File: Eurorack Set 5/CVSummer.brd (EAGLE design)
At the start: 19 x 106.5 mm, 35 parts, among them IC2 TL074D

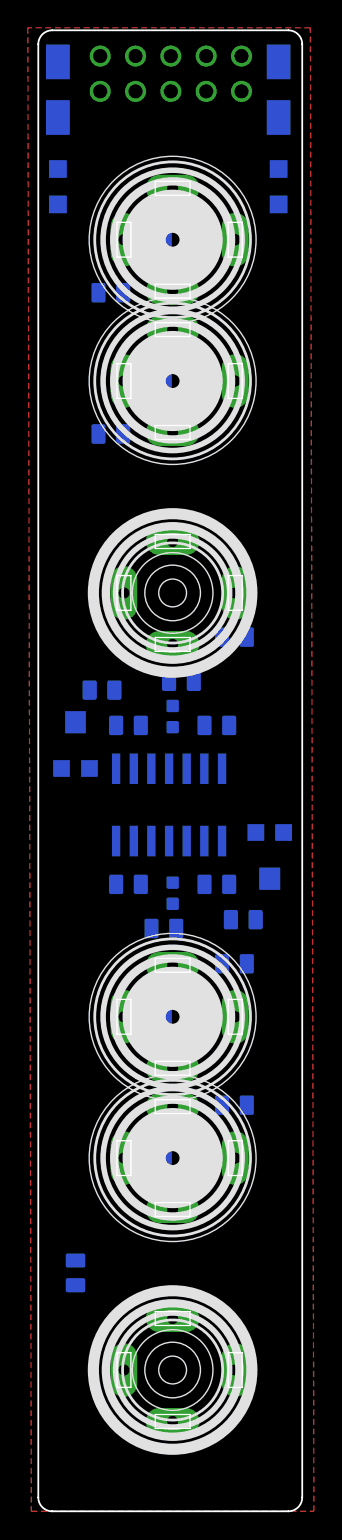
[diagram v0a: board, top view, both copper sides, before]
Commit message: Summer and Envelope updates (leftover opamp wiring)
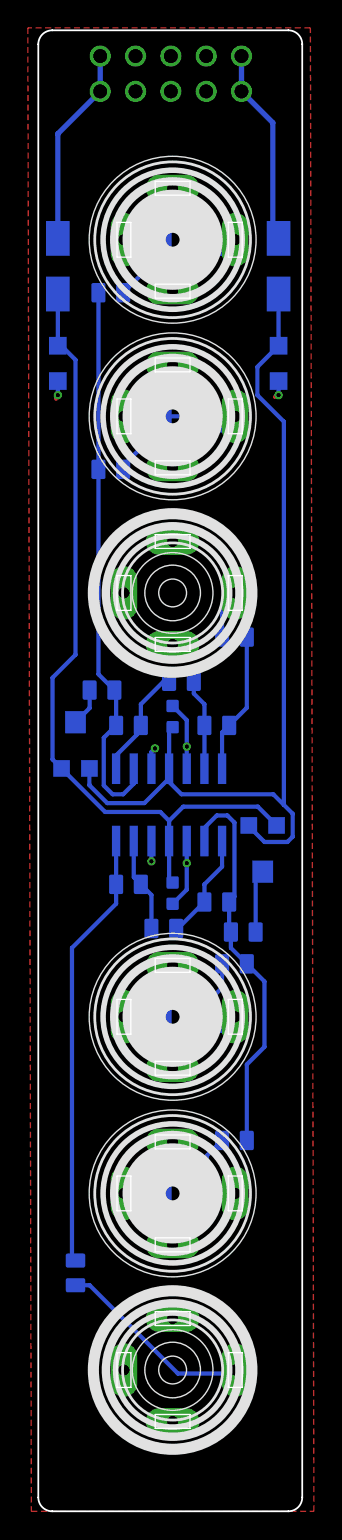
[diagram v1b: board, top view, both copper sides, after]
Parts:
- moved C11 12.7 mm to (1.91, 82.5)
- moved C12 12.7 mm to (17.8, 82.5)
- moved D1 12.7 mm to (1.91, 89.5)
- moved D2 12.7 mm to (17.8, 89.5)
- moved U$14 2.54 mm to (10.8, 78.7)
- moved U$2 2.54 mm to (10.2, 78.7)
- moved R8 2.54 mm to (14.6, 26.7)
- moved U$5 2.54 mm to (10.8, 22.9)
- moved U$6 2.54 mm to (10.2, 22.9)
- moved R5 2.54 mm to (5.71, 74.9)
- moved R2 1.27 mm to (13.3, 43.8)
- moved R6 0.89 mm to (15.2, 41.7)
- moved U$8 0.72 mm to (16.6, 47.5)
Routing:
- net -12V: track 0.00 -> 65.7 mm
- net 12V: track 0.00 -> 58.3 mm
- net N$14: track 0.00 -> 41.1 mm
- net N$5: track 0.00 -> 31.6 mm
- net N$13: track 0.00 -> 28.3 mm
- net GND: track 0.00 -> 15.7 mm, vias 0 -> 6
- net N$28: track 0.00 -> 14.4 mm
- net N$15: track 0.00 -> 14.2 mm
- net N$64: track 0.00 -> 14.2 mm
- net N$2: track 0.00 -> 10.2 mm
- net N$10: track 0.00 -> 8.66 mm
- net N$3: track 0.00 -> 8.66 mm
- net N$7: track 0.00 -> 8.09 mm
- net N$18: track 0.00 -> 7.73 mm
- net N$16: track 0.00 -> 7.00 mm
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
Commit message: Many tweaks for frontpanel setup
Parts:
- added SJ1, SJ2, SJ3, SJ4: SOLDERJUMPERNO, SparkFun-Passives:SJ_2S-NO
- moved C12 1.71 mm to (16.5, 83.7), turned to 180 degrees
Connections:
- new net N$20: SJ1.2, U$14.3, U$2.TIP@3
- new net N$21: SJ3.1, SJ4.1, U$3.SWITCH@3
- net GND: now also SJ2.1, SJ4.2; no longer U$3.SWITCH@3, U$6.SWITCH@3
- net N$1: now also SJ1.1, SJ2.2, U$6.SWITCH@3; no longer U$14.3, U$2.TIP@3
- net N$12: now also SJ3.2
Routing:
- net N$21: track 0.00 -> 68.1 mm, vias 0 -> 4
- net N$1: track 2.45 -> 67.6 mm, vias 0 -> 4
- net N$20: track 0.00 -> 5.40 mm
- net N$12: track 2.45 -> 5.23 mm
- net GND: track 15.7 -> 18.2 mm, vias 6 -> 8
- net -12V: track 65.7 -> 64.4 mm
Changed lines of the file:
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@@
 </element>
 <element name="C11" library="OPL" package="AVX-A" value="" x="1.905" y="82.55" rot="MR270"/>
-<element name="C12" library="OPL" package="AVX-A" value="" x="17.78" y="82.55" rot="MR90"/>
+<element name="C12" library="OPL" package="AVX-A" value="" x="16.51" y="83.693" rot="MR180"/>
 <element name="U$3" library="EurorackModularParts" package="3.5MM-JACK-SWITCH-13MM-INPUT" value="PJ-341" x="10.16" y="35.56" rot="R270">
 <attribute name="DESC" value="Input B" x="10.16" y="35.56" size="1.778" layer="27" rot="R270" display="off"/>
@@
 <element name="R13" library="OPL" package="C0805" value="100K" x="9.525" y="41.91" rot="MR0"/>
 <element name="R14" library="OPL" package="C0805" value="100K" x="6.985" y="45.085" rot="MR0"/>
+<element name="SJ1" library="SparkFun-Passives" package="SJ_2S-NO" value="SOLDERJUMPERNO" x="13.716" y="75.057" rot="MR0"/>
+<element name="SJ2" library="SparkFun-Passives" package="SJ_2S-NO" value="SOLDERJUMPERNO" x="6.731" y="19.05" rot="MR180"/>
+<element name="SJ3" library="SparkFun-Passives" package="SJ_2S-NO" value="SOLDERJUMPERNO" x="13.589" y="87.884" rot="MR0"/>
+<element name="SJ4" library="SparkFun-Passives" package="SJ_2S-NO" value="SOLDERJUMPERNO" x="6.731" y="31.877" rot="MR0"/>
 </elements>
 <signals>
@@
 <contactref element="IC2" pad="3"/>
 <contactref element="IC2" pad="5"/>
-<contactref element="U$6" pad="SWITCH@3"/>
 <contactref element="U$6" pad="RING@3"/>
 <contactref element="U$3" pad="RING@3"/>
-<contactref element="U$3" pad="SWITCH@3"/>
 <wire x1="11.176" y1="54.991" x2="11.176" y2="56.896" width="0.3048" layer="16"/>
 <wire x1="11.176" y1="56.896" x2="10.16" y2="57.912" width="0.3048" layer="16"/>
@@
 <wire x1="1.905" y1="80.264" x2="1.905" y2="80.137" width="0.3048" layer="1"/>
 <wire x1="1.905" y1="80.137" x2="1.778" y2="80.01" width="0.3048" layer="1"/>
-<wire x1="17.78" y1="81.28" x2="17.78" y2="80.264" width="0.3048" layer="16"/>
-<via x="17.78" y="80.264" extent="1-16" drill="0.3048"/>
-<wire x1="17.78" y1="80.264" x2="17.653" y2="80.264" width="0.3048" layer="1"/>
-<wire x1="17.653" y1="80.264" x2="17.526" y2="80.137" width="0.3048" layer="1"/>
+<wire x1="15.24" y1="83.693" x2="15.24" y2="84.836" width="0.3048" layer="16"/>
+<via x="15.24" y="84.836" extent="1-16" drill="0.3048"/>
+<wire x1="15.24" y1="84.836" x2="15.494" y2="85.09" width="0.3048" layer="1"/>
+<wire x1="15.494" y1="85.09" x2="15.24" y2="85.344" width="0.3048" layer="1"/>
+<contactref element="SJ2" pad="1"/>
+<contactref element="SJ4" pad="2"/>
+<wire x1="6.281" y1="31.877" x2="5.588" y2="31.877" width="0.3048" layer="16"/>
+<via x="5.588" y="31.877" extent="1-16" drill="0.3048"/>
+<wire x1="5.588" y1="31.877" x2="5.461" y2="31.877" width="0.3048" layer="1"/>
+<wire x1="5.461" y1="31.877" x2="5.334" y2="32.004" width="0.3048" layer="1"/>
+<wire x1="6.281" y1="19.05" x2="5.588" y2="19.05" width="0.3048" layer="16"/>
+<via x="5.588" y="19.05" extent="1-16" drill="0.3048"/>
+<wire x1="5.588" y1="19.05" x2="5.334" y2="19.05" width="0.3048" layer="1"/>
 </signal>
 <signal name="12V">
@@
 <wire x1="17.399" y1="51.562" x2="10.795" y2="51.562" width="0.3048" layer="16"/>
 <wire x1="10.795" y1="51.562" x2="9.779" y2="52.578" width="0.3048" layer="16"/>
-<wire x1="18.161" y1="50.8" x2="18.161" y2="78.359" width="0.3048" layer="16"/>
-<wire x1="17.78" y1="83.82" x2="17.78" y2="87.535" width="0.3048" layer="16"/>
-<wire x1="17.78" y1="83.82" x2="16.256" y2="82.296" width="0.3048" layer="16"/>
-<wire x1="16.256" y1="82.296" x2="16.256" y2="80.264" width="0.3048" layer="16"/>
-<wire x1="16.256" y1="80.264" x2="18.161" y2="78.359" width="0.3048" layer="16"/>
+<wire x1="18.161" y1="50.8" x2="18.161" y2="82.423" width="0.3048" layer="16"/>
+<wire x1="17.78" y1="83.693" x2="17.78" y2="87.535" width="0.3048" layer="16"/>
+<wire x1="17.78" y1="83.693" x2="17.78" y2="82.804" width="0.3048" layer="16"/>
+<wire x1="17.78" y1="82.804" x2="18.161" y2="82.423" width="0.3048" layer="16"/>
 </signal>
 <signal name="N$64" class="1">
@@
 <wire x1="1.905" y1="99.06" x2="4.953" y2="102.108" width="0.381" layer="16"/>
 </signal>
-<signal name="N$1">
-<contactref element="U$14" pad="3"/>
-<contactref element="U$2" pad="TIP@3"/>
-<wire x1="12.62" y1="77.74" x2="13.66" y2="77.74" width="0.3048" layer="16"/>
-<wire x1="13.66" y1="77.74" x2="14.66" y2="78.74" width="0.3048" layer="16"/>
-</signal>
 <signal name="N$2">
 <contactref element="R10" pad="1"/>
@@
 <wire x1="12.62" y1="90.44" x2="13.66" y2="90.44" width="0.3048" layer="16"/>
 <wire x1="13.66" y1="90.44" x2="14.66" y2="91.44" width="0.3048" layer="16"/>
+<contactref element="SJ3" pad="2"/>
+<wire x1="13.139" y1="87.884" x2="13.139" y2="89.921" width="0.3048" layer="16"/>
+<wire x1="13.139" y1="89.921" x2="12.62" y2="90.44" width="0.3048" layer="16"/>
 </signal>
 <signal name="N$14">
@@
 <wire x1="7.366" y1="45.593" x2="7.366" y2="48.2" width="0.3048" layer="16"/>
 </signal>
+<signal name="N$20">
+<contactref element="U$14" pad="3"/>
+<contactref element="U$2" pad="TIP@3"/>
+<wire x1="12.62" y1="77.74" x2="13.66" y2="77.74" width="0.3048" layer="16"/>
+<wire x1="13.66" y1="77.74" x2="14.66" y2="78.74" width="0.3048" layer="16"/>
+<contactref element="SJ1" pad="2"/>
+<wire x1="13.266" y1="75.057" x2="13.266" y2="77.094" width="0.3048" layer="16"/>
+<wire x1="13.266" y1="77.094" x2="12.62" y2="77.74" width="0.3048" layer="16"/>
+</signal>
+<signal name="N$1">
+<contactref element="U$6" pad="SWITCH@3"/>
+<contactref element="SJ1" pad="1"/>
+<contactref element="SJ2" pad="2"/>
+<wire x1="10.16" y1="19.16" x2="7.291" y2="19.16" width="0.3048" layer="16"/>
+<wire x1="7.291" y1="19.16" x2="7.181" y2="19.05" width="0.3048" layer="16"/>
+<wire x1="14.166" y1="75.057" x2="16.891" y2="72.332" width="0.3048" layer="16"/>
+<wire x1="16.891" y1="72.332" x2="16.891" y2="54.737" width="0.3048" layer="16"/>
+<wire x1="16.891" y1="54.737" x2="16.002" y2="53.848" width="0.3048" layer="16"/>
+<via x="16.002" y="53.848" extent="1-16" drill="0.3048"/>
+<wire x1="16.002" y1="53.848" x2="16.002" y2="45.847" width="0.3048" layer="1"/>
+<wire x1="16.002" y1="45.847" x2="17.399" y2="44.45" width="0.3048" layer="1"/>
+<via x="17.399" y="44.45" extent="1-16" drill="0.3048"/>
+<wire x1="17.399" y1="44.45" x2="17.399" y2="34.036" width="0.3048" layer="16"/>
+<via x="17.399" y="34.036" extent="1-16" drill="0.3048"/>
+<wire x1="17.399" y1="34.036" x2="17.399" y2="33.274" width="0.3048" layer="1"/>
+<wire x1="17.399" y1="33.274" x2="18.161" y2="32.512" width="0.3048" layer="1"/>
+<via x="18.161" y="32.512" extent="1-16" drill="0.3048"/>
+<wire x1="18.161" y1="32.512" x2="18.161" y2="22.098" width="0.3048" layer="16"/>
+<wire x1="18.161" y1="22.098" x2="15.223" y2="19.16" width="0.3048" layer="16"/>
+<wire x1="15.223" y1="19.16" x2="10.16" y2="19.16" width="0.3048" layer="16"/>
+</signal>
+<signal name="N$21">
+<contactref element="U$3" pad="SWITCH@3"/>
+<contactref element="SJ3" pad="1"/>
+<contactref element="SJ4" pad="1"/>
+<wire x1="10.16" y1="31.86" x2="7.198" y2="31.86" width="0.3048" layer="16"/>
+<wire x1="7.198" y1="31.86" x2="7.181" y2="31.877" width="0.3048" layer="16"/>
+<wire x1="14.039" y1="87.884" x2="16.637" y2="85.286" width="0.3048" layer="16"/>
+<wire x1="16.637" y1="85.286" x2="16.637" y2="82.423" width="0.3048" layer="16"/>
+<wire x1="16.637" y1="82.423" x2="17.526" y2="81.534" width="0.3048" layer="16"/>
+<wire x1="17.526" y1="81.534" x2="17.526" y2="52.832" width="0.3048" layer="16"/>
+<wire x1="17.526" y1="52.832" x2="17.272" y2="52.578" width="0.3048" layer="16"/>
+<via x="17.272" y="52.578" extent="1-16" drill="0.3048"/>
+<wire x1="17.272" y1="52.578" x2="17.272" y2="47.625" width="0.3048" layer="1"/>
+<wire x1="17.272" y1="47.625" x2="18.288" y2="46.609" width="0.3048" layer="1"/>
+<via x="18.288" y="46.609" extent="1-16" drill="0.3048"/>
+<wire x1="18.288" y1="46.609" x2="18.288" y2="33.655" width="0.3048" layer="16"/>
+<wire x1="18.288" y1="33.655" x2="16.51" y2="31.877" width="0.3048" layer="16"/>
+<via x="16.51" y="31.877" extent="1-16" drill="0.3048"/>
+<wire x1="16.51" y1="31.877" x2="14.478" y2="31.877" width="0.3048" layer="1"/>
+<via x="14.478" y="31.877" extent="1-16" drill="0.3048"/>
+<wire x1="14.478" y1="31.877" x2="14.461" y2="31.86" width="0.3048" layer="16"/>
+<wire x1="14.461" y1="31.86" x2="10.16" y2="31.86" width="0.3048" layer="16"/>
+</signal>
 </signals>

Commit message: Doublechecks & artwork prep
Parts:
- C1, C2: value (none) -> 100nF
- C11, C12: value (none) -> 10uF
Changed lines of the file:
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@@
 <?xml version="1.0" encoding="utf-8"?>
 <!DOCTYPE eagle SYSTEM "eagle.dtd">
-<eagle version="6.5.0">
+<eagle version="7.7.0">
 <drawing>
 <settings>
@@
 <pass name="Default">
 <param name="RoutingGrid" value="4.92125984mil"/>
+<param name="AutoGrid" value="1"/>
+<param name="Efforts" value="0"/>
+<param name="TopRouterVariant" value="1"/>
 <param name="tpViaShape" value="round"/>
 <param name="PrefDir.1" value="*"/>
@@
 <element name="IC2" library="EurorackModularParts" package="SO14" value="TL074D" x="9.906" y="50.8" rot="MR0"/>
 <element name="U$10" library="EurorackModularParts" package="POWER_10" value="POWER_SIMPLE10" x="10.033" y="103.378" rot="MR0"/>
-<element name="C1" library="OPL" package="C0603" value="" x="10.16" y="44.45" rot="MR90"/>
-<element name="C2" library="OPL" package="C0603" value="" x="10.16" y="57.15" rot="MR90"/>
+<element name="C1" library="OPL" package="C0603" value="100nF" x="10.16" y="44.45" rot="MR90"/>
+<element name="C2" library="OPL" package="C0603" value="100nF" x="10.16" y="57.15" rot="MR90"/>
 <element name="D1" library="OPL" package="DO-214AC" value="MRA4004T3G" x="1.905" y="89.535" rot="MR270">
 <attribute name="MPN" value="US1G-E3/5AT" x="1.905" y="89.535" size="1.778" layer="28" rot="MR270" display="off"/>
@@
 <attribute name="OC_FARNELL" value="9551824" x="17.78" y="89.535" size="1.778" layer="28" rot="MR90" display="off"/>
 </element>
-<element name="C11" library="OPL" package="AVX-A" value="" x="1.905" y="82.55" rot="MR270"/>
-<element name="C12" library="OPL" package="AVX-A" value="" x="16.51" y="83.693" rot="MR180"/>
+<element name="C11" library="OPL" package="AVX-A" value="10uF" x="1.905" y="82.55" rot="MR270"/>
+<element name="C12" library="OPL" package="AVX-A" value="10uF" x="16.51" y="83.693" rot="MR180"/>
 <element name="U$3" library="EurorackModularParts" package="3.5MM-JACK-SWITCH-13MM-INPUT" value="PJ-341" x="10.16" y="35.56" rot="R270">
 <attribute name="DESC" value="Input B" x="10.16" y="35.56" size="1.778" layer="27" rot="R270" display="off"/>
